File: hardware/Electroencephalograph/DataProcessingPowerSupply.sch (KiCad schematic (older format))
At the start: 5 parts, among them J6 Conn_01x02_Female, U11 L78L33_SO8

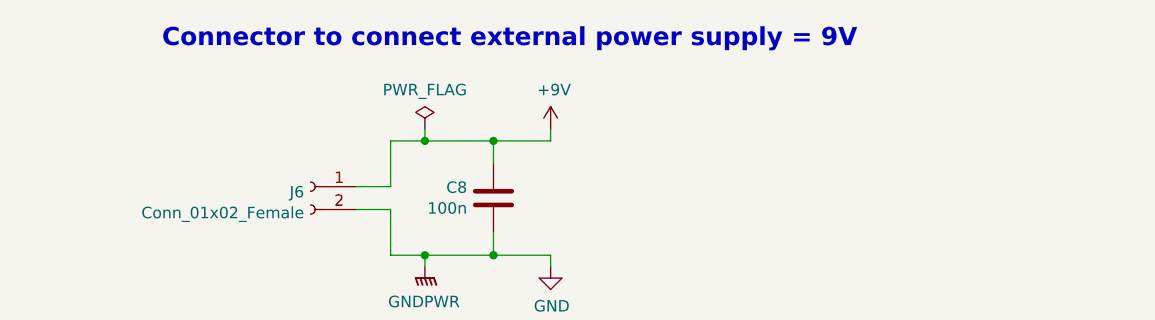
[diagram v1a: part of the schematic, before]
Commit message: add support for esp module
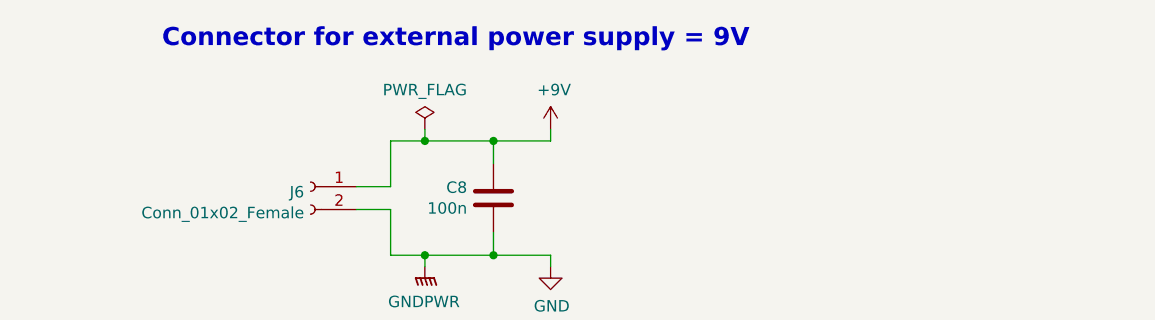
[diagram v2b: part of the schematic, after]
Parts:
- J6: footprint (none) -> Connector_PinHeader_2.54mm:PinHeader_1x02_P2.54mm_Vertical
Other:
- note added: "Connector for external power supply = 9V"
- note removed: "Connector to connect external power supply = 9V"
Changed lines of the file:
@@
 F 0 "J6" H 2078 1726 50  0000 L CNN
 F 1 "Conn_01x02_Female" H 2078 1635 50  0000 L CNN
-F 2 "" H 2050 1750 50  0001 C CNN
+F 2 "Connector_PinHeader_2.54mm:PinHeader_1x02_P2.54mm_Vertical" H 2050 1750 50  0001 C CNN
 F 3 "~" H 2050 1750 50  0001 C CNN
 	1    2050 1750
@@
 Connection ~ 2850 1550
 Text Notes 1400 1150 0    79   ~ 16
-Connector to connect external power supply = 9V
+Connector for external power supply = 9V
 Wire Wire Line
 	3000 3900 3250 3900
